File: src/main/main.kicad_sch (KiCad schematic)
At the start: 14 parts, among them J101 Conn_02x05_Odd_Even, P101 SMTSO3035CTJ, P102 SMTSO3035CTJ, P103 SMTSO3035CTJ, P104 SMTSO3035CTJ, U101 LTV-817S

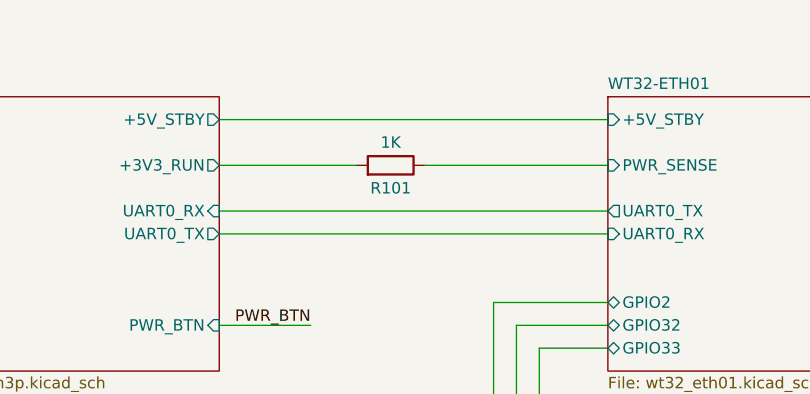
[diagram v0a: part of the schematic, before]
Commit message: rev1.1.0
- J201 programming header
  - Add reset button
  - Add enable button
  - Make pinout compatible with USB-UART boards
    - Move GPI0 and ENABLE to testpoints
- Add power rail LED status indicators
  - 3V3_RUN
  - 3V3_ESP32
  - 5V_RUN
  - 5V_STBY
  - VBUS_[1-3]
- Remove JP201
- Add GPIO39 external pullup to 3V3
- Add pulldown to PWR_BUTTON (GPIO15)
- Add github link
- Add sillkscreen alignment fixes
- Add silkscreen default jumper marking
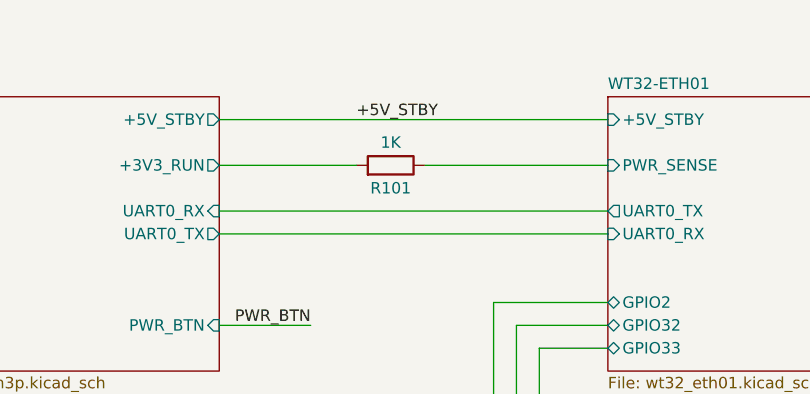
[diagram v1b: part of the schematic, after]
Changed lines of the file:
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@@
     (effects (font (size 1.27 1.27)) (justify right bottom))
+  )
+  (label "+5V_STBY" (at 147.32 46.99 0) (fields_autoplaced)
+    (effects (font (size 1.27 1.27)) (justify left bottom))
   )
   (label "PWR_BTN" (at 257.81 133.35 180) (fields_autoplaced)

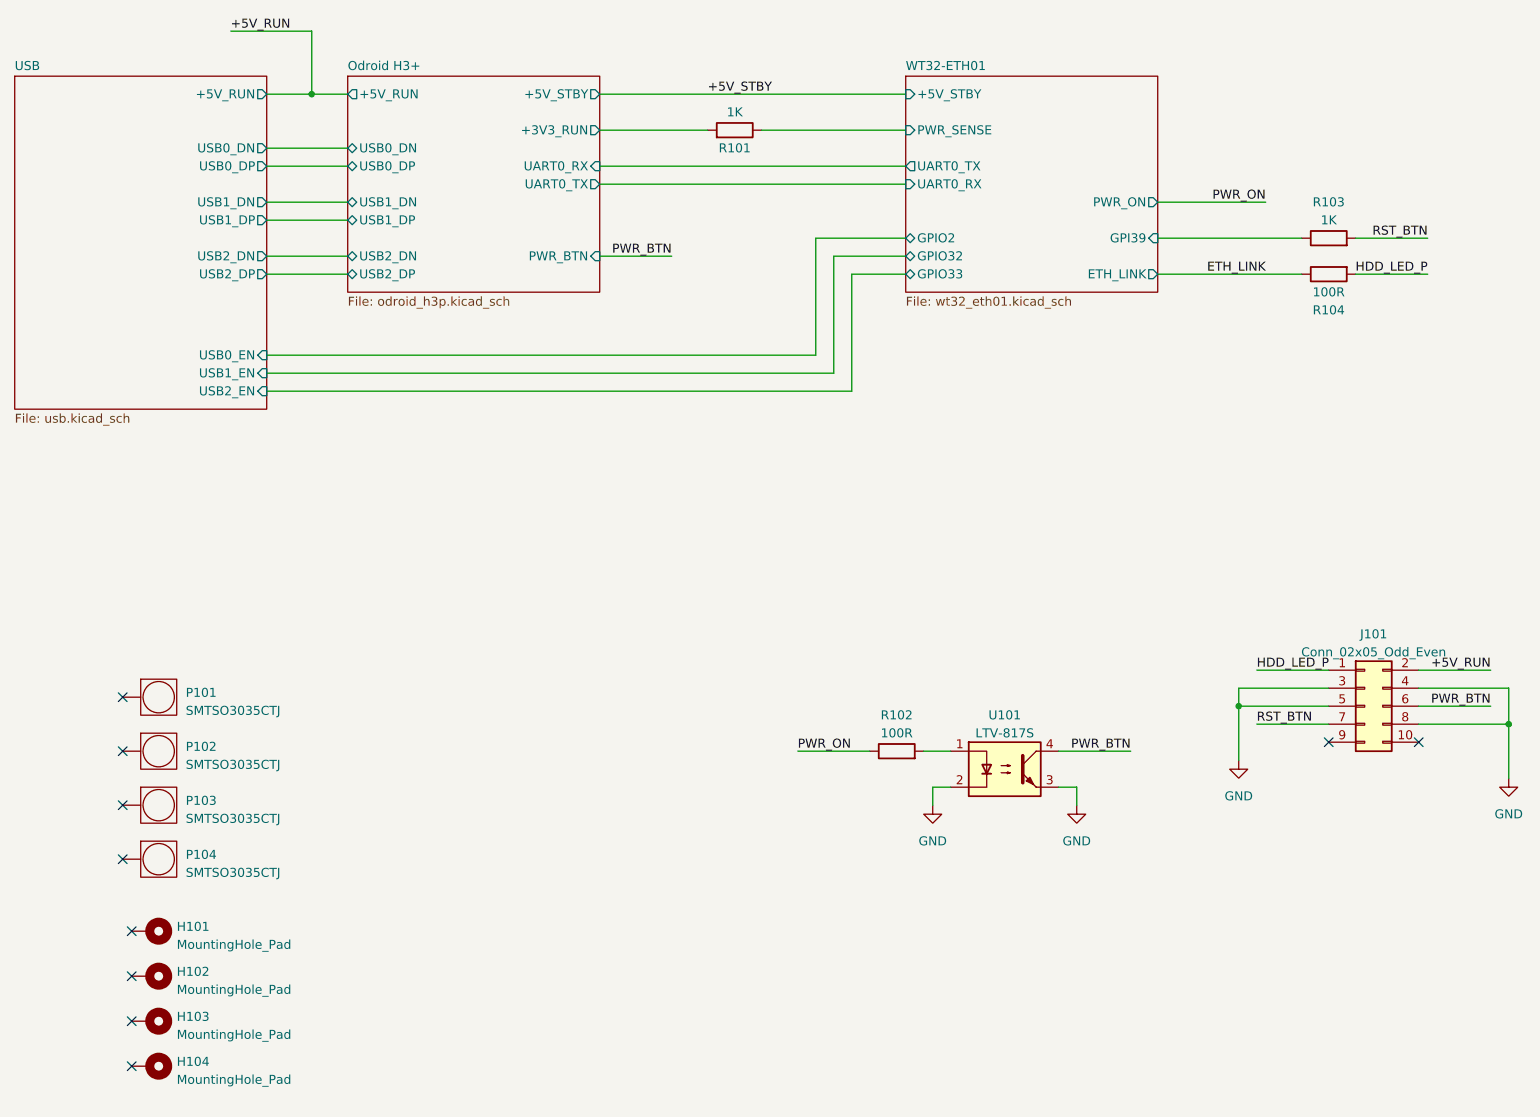
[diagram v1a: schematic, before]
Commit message: Additions and fixes:
Add:
- Add power rail LED status indicators
- Buffered LED on ETH_LINK
- GPIO14 and GPIO12 on header
- GPIO14 5V buffered output on header
- Testpoints for GPIO0 and ESP32_ENABLE pin
- Reset and Boot switches
- ESP PWR selector switch
- USB Type-C PD input (5V) for ESP32
- 1.1A Fuse for USB PD input
- Add spot for BIOS battery on silk
- Add silkscreen default jumper marking
- Add GPIO39 external pullup to 3V3
- Add pulldown to PWR_BUTTON (GPIO15)
- Add silkscreen github link

Fixes:
- Clarify things on silk
- Make pinout compatible with USB-UART boards
  - Move GPI0 and ENABLE to testpoints
- Silkscreen alignment fixes

Removed:
- 3 APA102 LEDs
- Remove JP201
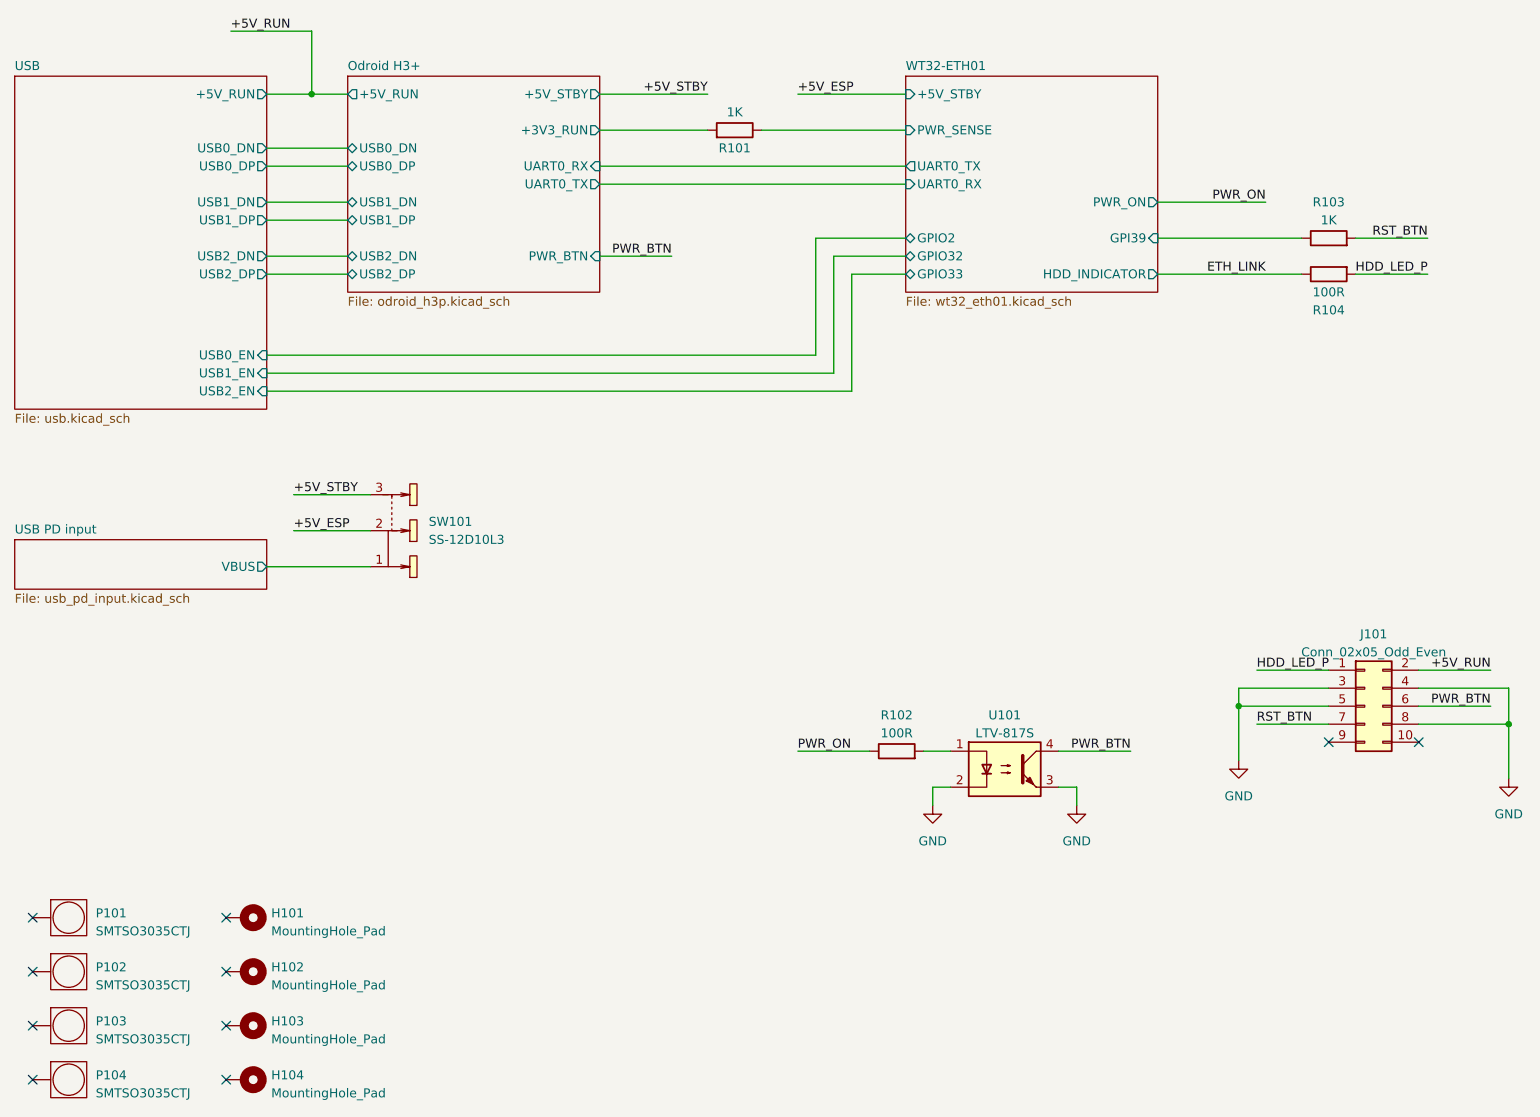
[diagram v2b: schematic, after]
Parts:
- added SW101: SS-12D10L3, easyeda2kicad:SW-TH_SS-12D10L3, symbol easyeda2kicad:SS-12D10L3
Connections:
- net +5V_STBY: now also SW101.3
- new net +5V_ESP: SW101.2
- new net USB PD input/VBUS: SW101.1
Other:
- added sheet USB PD input (usb_pd_input.kicad_sch)
- sheet WT32-ETH01 ports: added HDD_INDICATOR; removed ETH_LINK
- moved on the sheet: H101, H102, H103, H104, P101, P102, P103, P104
